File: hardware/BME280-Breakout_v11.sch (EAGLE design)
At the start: 23 parts, among them IC1 BME280, IC2 LDO-TS9011-3V3, J1 JUMPER2-0603, T1 BSS138PS, T2 BSS138PS, X1 PASSER-07, X2 PASSER-07

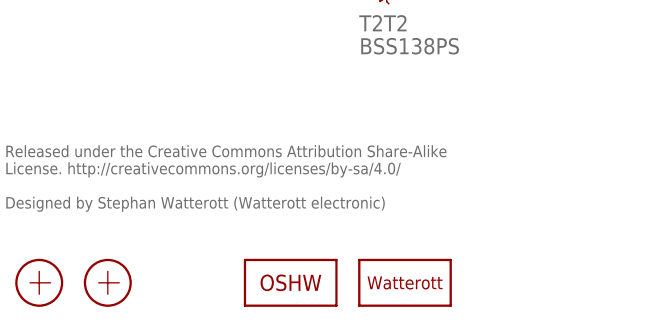
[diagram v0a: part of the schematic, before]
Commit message: updated schematics
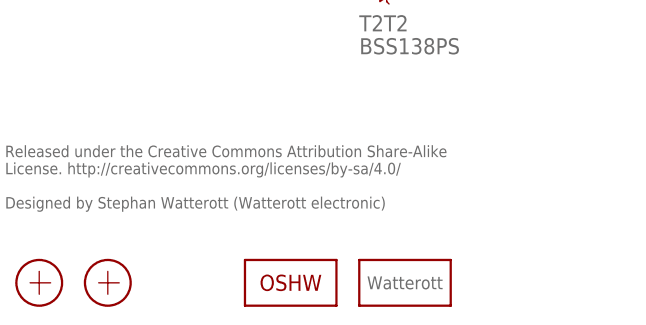
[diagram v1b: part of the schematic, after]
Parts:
- removed LOGO1: LOGO-S_PLACE_S, we-symbol:LOGO-S_PLACE_S
- added LOGO3: LOGO_SPARK-2, we-symbol:LOGO_SPARK-2
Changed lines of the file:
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@@
 <setting verticaltext="up"/>
 </settings>
-<grid distance="0.1" unitdist="inch" unit="inch" style="lines" multiple="1" display="no" altdistance="0.01" altunitdist="inch" altunit="inch"/>
+<grid distance="0.05" unitdist="inch" unit="inch" style="lines" multiple="1" display="yes" altdistance="0.01" altunitdist="inch" altunit="inch"/>
 <layers>
 <layer number="1" name="Top" color="4" fill="1" visible="no" active="no"/>
@@
 <part name="X1" library="we-symbol" deviceset="PASSER" device="-07"/>
 <part name="X2" library="we-symbol" deviceset="PASSER" device="-07"/>
-<part name="LOGO1" library="we-symbol" deviceset="LOGO" device="-S_PLACE_S"/>
 <part name="LOGO2" library="we-symbol" deviceset="OSHW_LOGO" device="X0070"/>
 <part name="J1" library="we-rcl" deviceset="JUMPER2" device="-0603"/>
 <part name="GND8" library="supply1" deviceset="GND" device=""/>
 <part name="HOUSING1" library="we-sensor" deviceset="SF2" device=""/>
+<part name="LOGO3" library="we-symbol" deviceset="LOGO_SPARK" device="-2"/>
 </parts>
 <sheets>
@@
 <instance part="X1" gate="X" x="166.37" y="7.62"/>
 <instance part="X2" gate="X" x="173.99" y="7.62"/>
-<instance part="LOGO1" gate="L" x="207.01" y="7.62"/>
 <instance part="LOGO2" gate="L" x="194.31" y="7.62"/>
 <instance part="J1" gate="J" x="88.9" y="129.54" rot="R90"/>
 <instance part="GND8" gate="1" x="88.9" y="119.38"/>
 <instance part="HOUSING1" gate="G$1" x="66.04" y="144.78"/>
+<instance part="LOGO3" gate="G$1" x="207.01" y="7.62"/>
 </instances>
 <busses>

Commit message: updated schematics
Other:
- note added: "I2C Address SDO high = 0x77 SDO low = 0x76"
- note removed: "I2C Address open = 0x77 closed = 0x76"
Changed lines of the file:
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@@
 <sheet>
 <plain>
-<text x="91.44" y="124.46" size="1.778" layer="91">I2C Address
-open   = 0x77
-closed = 0x76</text>
+<text x="91.44" y="152.4" size="1.778" layer="91">I2C Address
+SDO high = 0x77
+SDO low = 0x76</text>
 <text x="162.56" y="22.86" size="1.27" layer="95" align="top-left">Released under the Creative Commons Attribution Share-Alike
 License. http://creativecommons.org/licenses/by-sa/4.0/
